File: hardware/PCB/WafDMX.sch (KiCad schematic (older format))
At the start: 16 parts

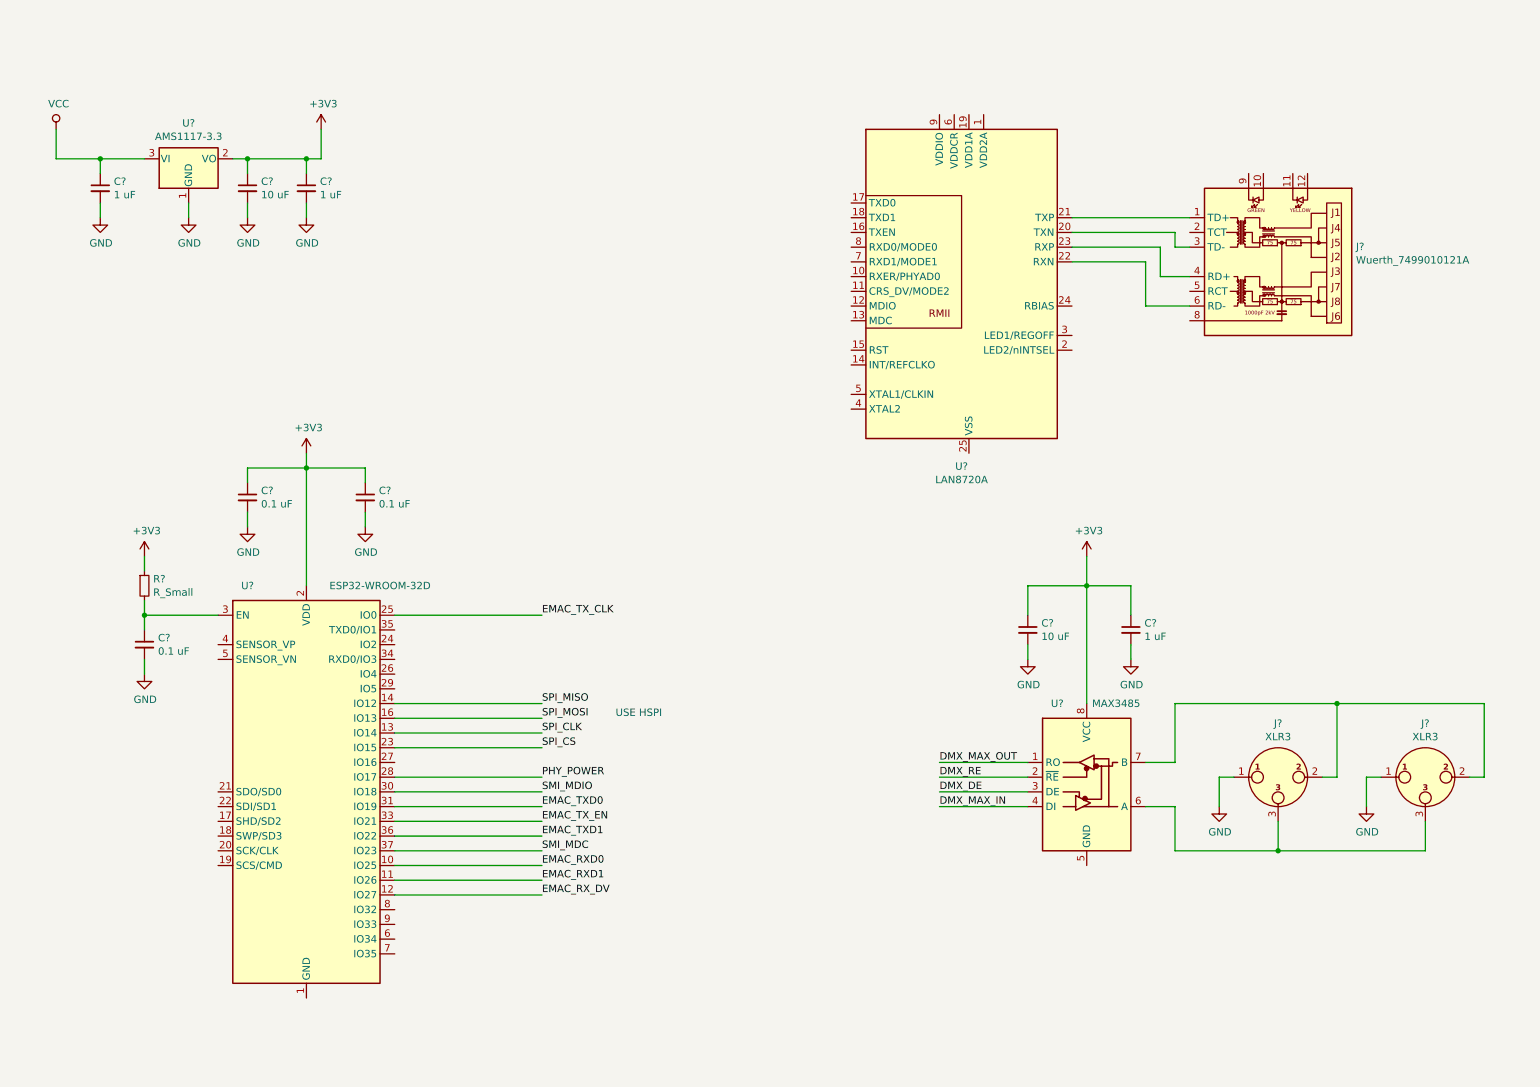
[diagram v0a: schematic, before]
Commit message: Add LAN8720A and trace
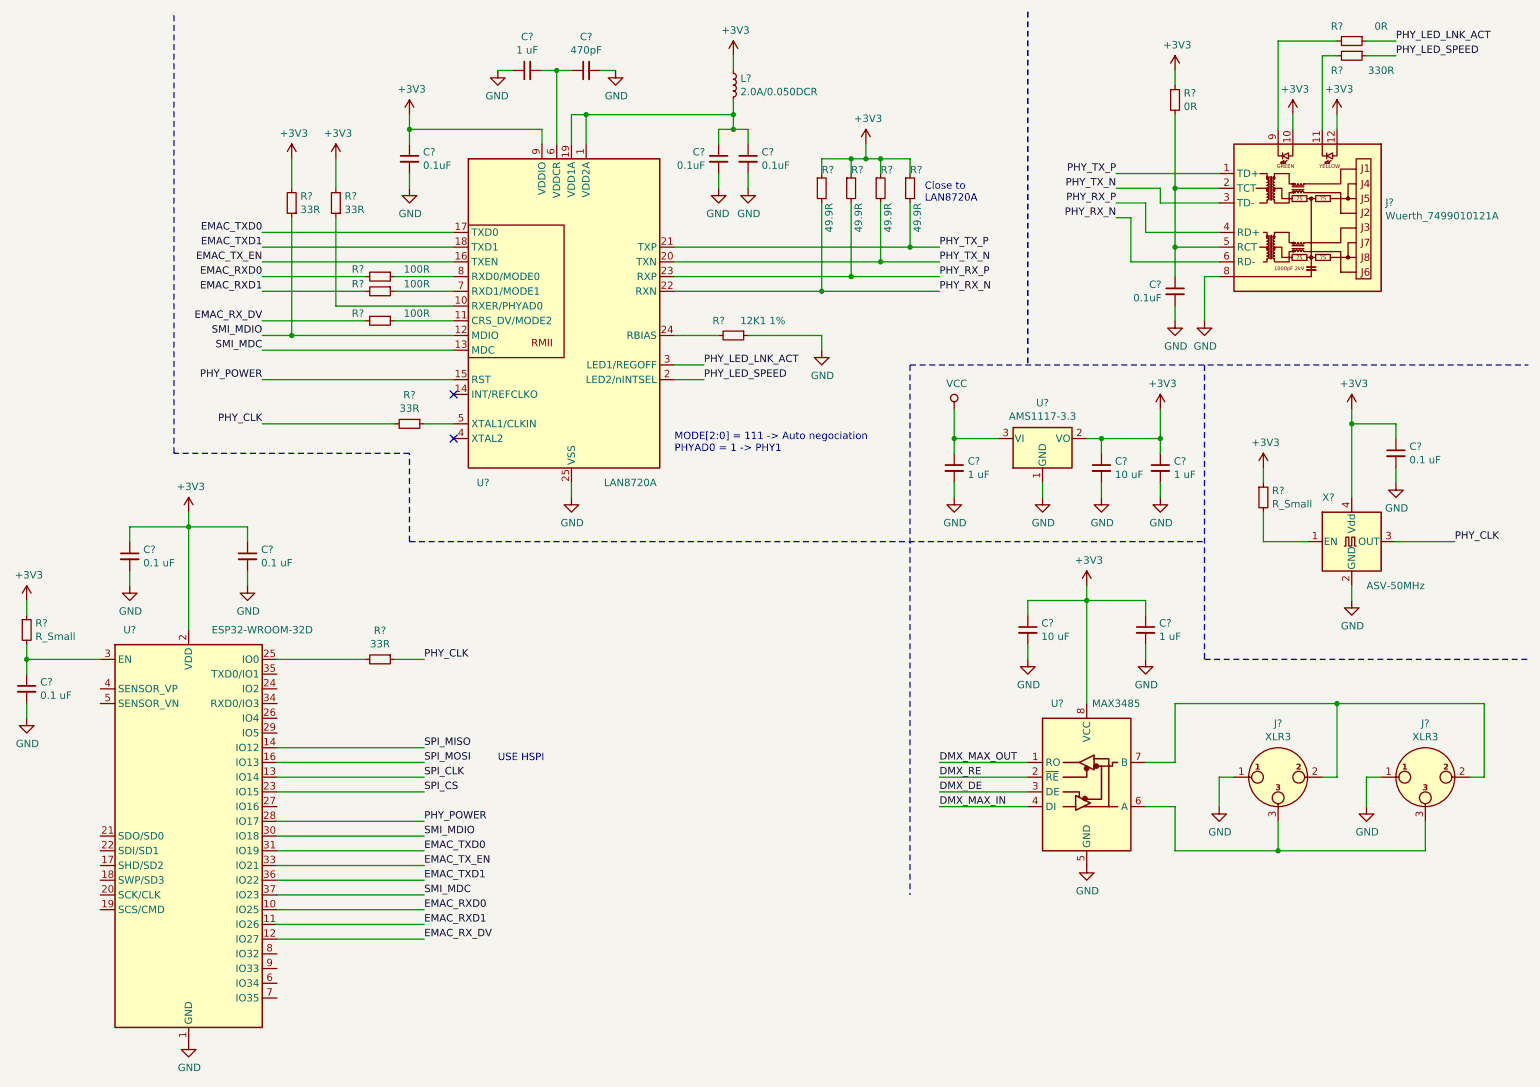
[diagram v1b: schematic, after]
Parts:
- added C? (x4): 0.1uF, symbol Device:C_Small
- added C?: 0.1 uF, symbol Device:C_Small
- added C?: 470pF, symbol Device:C_Small
- added C?: 1 uF, symbol Device:C_Small
- added L?: 2.0A/0.050DCR, symbol Device:L_Small
- added R? (x2): 0R, symbol Device:R_Small
- added R?: 330R, symbol Device:R_Small
- added R?: 12K1 1%, symbol Device:R_Small
- added R?: R_Small, symbol Device:R_Small
- added R? (x4): 33R, symbol Device:R_Small
- added R? (x4): 49.9R, symbol Device:R_Small
- added R? (x3): 100R, symbol Device:R_Small
- added X?: ASV-50MHz, Oscillator:Oscillator_SMD_Abracon_ASE-4Pin_3.2x2.5mm_HandSoldering, symbol Oscillator:ASV-xxxMHz
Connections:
- net +3V3: now also J?.10, J?.12, U?.9 (VDDIO), C?.1, C?.1, L?.1, R?.1, R?.1, R?.1, R?.1, R?.1, R?.1, R?.2, R?.2, X?.4 (Vdd)
- net EMAC_RXD0: now also R?.2
- net EMAC_RXD1: now also R?.2
- net EMAC_RX_DV: now also R?.2
- net EMAC_TXD0: now also U?.17 (TXD0)
- net EMAC_TXD1: now also U?.18 (TXD1)
- net EMAC_TX_EN: now also U?.16 (TXEN)
- net GND: now also J?.8, U?.1 (GND), U?.15 (GND), U?.25 (VSS), U?.38 (GND), U?.5 (GND), C?.1, C?.2, C?.2, C?.2, C?.2, C?.2, C?.2, R?.1, X?.2 (GND)
- net PHY_POWER: now also U?.15 (RST)
- net SMI_MDC: now also U?.13 (MDC)
- net SMI_MDIO: now also U?.12 (MDIO), R?.1
- net at U?.1 (VDD2A): now also U?.19 (VDD1A), C?.1, C?.1, L?.2
- net at U?.10 (RXER/PHYAD0): now also R?.1
- net at U?.11 (CRS_DV/MODE2): now also R?.1
- net PHY_LED_SPEED: now reaches U?.2 (LED2/nINTSEL)
- net PHY_LED_SPEED: now also R?.1
- net PHY_TX_N: now reaches J?.3 (TD-), U?.20 (TXN)
- net PHY_TX_N: now also R?.2
- net PHY_TX_P: now reaches J?.1 (TD+), U?.21 (TXP)
- net PHY_TX_P: now also R?.2
- net PHY_RX_N: now reaches J?.6 (RD-), U?.22 (RXN)
- net PHY_RX_N: now also R?.2
- net PHY_RX_P: now reaches J?.4 (RD+), U?.23 (RXP)
- net PHY_RX_P: now also R?.2
- net at U?.24 (RBIAS): now also R?.2
- net PHY_LED_LNK_ACT: now reaches U?.3 (LED1/REGOFF)
- net PHY_LED_LNK_ACT: now also R?.1
- net at U?.5 (XTAL1/CLKIN): now also R?.1
- net at U?.6 (VDDCR): now also C?.1, C?.2
- net at U?.7 (RXD1/MODE1): now also R?.1
- net at U?.8 (RXD0/MODE0): now also R?.1
- net at J?.11: now also R?.2
- net at J?.2 (TCT): now also J?.5 (RCT), C?.1, R?.2
- net at J?.9: now also R?.2
- net EMAC_TX_CLK: no longer names the net of U?.25 (IO0)
- net EMAC_TX_CLK: now also R?.2
- new net: R?.2, X?.1 (EN)
- new net PHY_CLK: R?.1, R?.2, X?.3 (OUT)
- no-connect marks 0 -> 2
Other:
- note added: "Close to\nLAN8720A"
- note added: "MODE[2:0] = 111 -> Auto negociation\nPHYAD0 = 1 -> PHY1\n"
- moved on the sheet: C?, J?, R?, U?

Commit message: Use A3 paper size, add CH340C
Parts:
- removed R? (x4): 49.9R, symbol Device:R_Small
- removed R? (x3): 100R, symbol Device:R_Small
- added C?: 0.01 uF, symbol Device:C_Small
- added C?: 0.1 uF, symbol Device:C_Small
- added C?: 22 uF, symbol Device:C_Small
- added J?: USB_B_Micro, Connector_USB:USB_Micro-B_Molex-105017-0001, symbol Connector:USB_B_Micro
- added J?: Screw_Terminal_01x02, TerminalBlock_Phoenix:TerminalBlock_Phoenix_MKDS-1,5-2_1x02_P5.00mm_Horizontal, symbol Connector:Screw_Terminal_01x02
- added Q? (x2): MMDT2222A, Package_TO_SOT_SMD:SOT-363_SC-70-6, symbol Transistor_BJT:MMDT2222A
- added R? (x2): 10K, symbol Device:R_Small
- added TP? (x13): TestPoint, TestPoint:TestPoint_Pad_1.0x1.0mm, symbol Connector:TestPoint
- added U?: CH340C, Package_SO:SOP-16_4.4x10.4mm_P1.27mm, symbol WafDMX:CH340C
- C?: value 10 uF -> 0.1 uF
- J?: footprint Connector_RJ:RJ45_Wuerth_7499151120_Horizontal -> Connector_RJ:RJ45_Wuerth_7499010121A_Horizontal
- R?: value R_Small -> 10K
- X?: footprint Oscillator:Oscillator_SMD_Abracon_ASE-4Pin_3.2x2.5mm_HandSoldering -> Oscillator:Oscillator_SMD_Abracon_ASV-4Pin_7.0x5.1mm
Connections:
- net +3V3: now also C?.1, C?.1, U?.16 (VCC); no longer R?.1
- net EMAC_RXD0: now also U?.8 (RXD0/MODE0)
- net EMAC_RXD1: now also U?.7 (RXD1/MODE1)
- net EMAC_RX_DV: now also U?.11 (CRS_DV/MODE2)
- net GND: now also R?.2, C?.2, C?.2, C?.2, J?.2 (Pin_2), J?.5 (GND), J?.6 (Shield), U?.1 (GND)
- net VCC: now also J?.1 (Pin_1)
- net at U?.17 (SHD/SD2): now also TP?.1
- net at U?.18 (SWP/SD3): now also TP?.1
- net at U?.19 (SCS/CMD): now also TP?.1
- net at U?.20 (SCK/CLK): now also TP?.1
- net at U?.21 (SDO/SD0): now also TP?.1
- net at U?.22 (SDI/SD1): now also TP?.1
- net at U?.24 (IO2): now also TP?.1
- net IO0: now reaches R?.2, U?.25 (IO0)
- net IO0: now also Q?.6 (C1)
- net at U?.26 (IO4): now also TP?.1
- net PHY_CLK_EN: now reaches U?.27 (IO16)
- net PHY_CLK_EN: now also R?.1, X?.1 (EN)
- net at U?.29 (IO5): now also TP?.1
- net EN: now reaches C?.1, R?.2, U?.3 (EN)
- net EN: now also Q?.4 (E2)
- net ESP32_RX: now reaches U?.34 (RXD0/IO3)
- net ESP32_RX: now also U?.2 (TXD)
- net ESP32_TX: now reaches U?.35 (TXD0/IO1)
- net ESP32_TX: now also U?.3 (RXD)
- net at U?.6 (IO34): now also TP?.1
- net at U?.7 (IO35): now also TP?.1
- net at U?.8 (IO32): now also TP?.1
- net at U?.9 (IO33): now also TP?.1
- new net: C?.1, U?.4 (V3)
- new net: Q?.2 (B1), R?.1
- new net: Q?.5 (B2), R?.1
- new net DTR: Q?.1 (E1), R?.2, U?.13 (DTR)
- new net RTS: Q?.3 (C2), R?.2, U?.14 (RTS)
- new net USB_DN: J?.2 (D-), U?.5 (UD_N)
- new net USB_DP: J?.3 (D+), U?.6 (UD_P)
- no-connect marks 2 -> 11
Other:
- note added: "All resistors MUST be close to LAN8720A"
- note removed: "Close to\nLAN8720A"
- moved on the sheet: C?, J?, L?, R?, U?, X?

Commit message: Place components
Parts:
- removed TP? (x4): TestPoint, TestPoint:TestPoint_Pad_1.0x1.0mm, symbol Connector:TestPoint
- added J4: Conn_01x04_Female, Connector_PinHeader_2.54mm:PinHeader_1x04_P2.54mm_Vertical, symbol Connector:Conn_01x04_Female
- added JP1: SolderJumper_2_Open, Jumper:SolderJumper-2_P1.3mm_Open_Pad1.0x1.5mm, symbol Jumper:SolderJumper_2_Open
- added P1, P2, P3, P4: POW_OUT, symbol WafDMX:POW_OUT
- added TP4, TP5: TestPoint, TestPoint:TestPoint_Pad_1.0x1.0mm, symbol Connector:TestPoint
- C1, C10, C11, C12, C14, C15, C16, C17, C18, C2, C6, C7, C9: renamed from C?; footprint (none) -> Capacitor_SMD:C_0603_1608Metric
- C13, C8: renamed from C?; footprint (none) -> Capacitor_SMD:C_1206_3216Metric
- C3, C4, C5: renamed from C?; value 0.1uF -> 0.1 uF; footprint (none) -> Capacitor_SMD:C_0603_1608Metric
- L1: renamed from L?; footprint (none) -> Inductor_SMD:L_0603_1608Metric
- R1, R10, R11, R12, R2, R3, R4, R5, R6, R7, R8: renamed from R?; footprint (none) -> Resistor_SMD:R_0603_1608Metric
- R9: renamed from R?; value R_Small -> 10K; footprint (none) -> Resistor_SMD:R_0603_1608Metric
- gave numbers to parts that had none: 21
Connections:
- net DMX_DE: now also U4.19 (SCS/CMD)
- net DMX_MAX_IN: now also U4.18 (SWP/SD3)
- net DMX_MAX_OUT: now also U4.17 (SHD/SD2)
- net DMX_RE: now also U4.20 (SCK/CLK)
- net GND: now also J2.1 (Pin_1), J4.4 (Pin_4); no longer J2.2 (Pin_2)
- net SPI_CLK: now also J4.2 (Pin_2)
- net SPI_MOSI: now also J4.3 (Pin_3)
- net VCC: now also J2.2 (Pin_2), JP1.1 (A), P1.~; no longer J2.1 (Pin_1)
- net at C4.1, C5.1, L1.2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: now also P4.~
- net at C1.2, C2.1, U2.6 (VDDCR): now also P2.~
- net at C11.1, U3.4 (V3): now also P3.~
- net SPI_CS: no longer names the net of U4.23 (IO15)
- net SPI_CS: now also TP5.1
- net SPI_MISO: no longer names the net of U4.14 (IO12)
- net SPI_MISO: now also TP4.1
- new net: J4.1 (Pin_1), JP1.2 (B)
- no-connect marks 11 -> 13
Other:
- moved on the sheet: J2

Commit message: Change Testpoints to TH, start placing
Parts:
- TP1, TP10, TP11, TP2, TP3, TP4, TP5, TP6, TP7, TP8, TP9: footprint TestPoint:TestPoint_Pad_1.0x1.0mm -> TestPoint:TestPoint_THTPad_1.0x1.0mm_Drill0.5mm
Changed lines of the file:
@@
 F 0 "TP1" V 4500 7300 50  0000 L CNN
 F 1 "TestPoint" V 4500 7575 50  0000 L CNN
-F 2 "TestPoint:TestPoint_Pad_1.0x1.0mm" H 4700 7100 50  0001 C CNN
+F 2 "TestPoint:TestPoint_THTPad_1.0x1.0mm_Drill0.5mm" H 4700 7100 50  0001 C CNN
 F 3 "~" H 4700 7100 50  0001 C CNN
 	1    4500 7100
@@
 F 0 "TP2" V 4500 7500 50  0000 L CNN
 F 1 "TestPoint" V 4500 7775 50  0000 L CNN
-F 2 "TestPoint:TestPoint_Pad_1.0x1.0mm" H 4700 7300 50  0001 C CNN
+F 2 "TestPoint:TestPoint_THTPad_1.0x1.0mm_Drill0.5mm" H 4700 7300 50  0001 C CNN
 F 3 "~" H 4700 7300 50  0001 C CNN
 	1    4500 7300
@@
 F 0 "TP3" V 4500 7600 50  0000 L CNN
 F 1 "TestPoint" V 4500 7875 50  0000 L CNN
-F 2 "TestPoint:TestPoint_Pad_1.0x1.0mm" H 4700 7400 50  0001 C CNN
+F 2 "TestPoint:TestPoint_THTPad_1.0x1.0mm_Drill0.5mm" H 4700 7400 50  0001 C CNN
 F 3 "~" H 4700 7400 50  0001 C CNN
 	1    4500 7400
@@
 F 0 "TP8" V 4500 9100 50  0000 L CNN
 F 1 "TestPoint" V 4500 9375 50  0000 L CNN
-F 2 "TestPoint:TestPoint_Pad_1.0x1.0mm" H 4700 8900 50  0001 C CNN
+F 2 "TestPoint:TestPoint_THTPad_1.0x1.0mm_Drill0.5mm" H 4700 8900 50  0001 C CNN
 F 3 "~" H 4700 8900 50  0001 C CNN
 	1    4500 8900
@@
 F 0 "TP9" V 4500 9200 50  0000 L CNN
 F 1 "TestPoint" V 4500 9475 50  0000 L CNN
-F 2 "TestPoint:TestPoint_Pad_1.0x1.0mm" H 4700 9000 50  0001 C CNN
+F 2 "TestPoint:TestPoint_THTPad_1.0x1.0mm_Drill0.5mm" H 4700 9000 50  0001 C CNN
 F 3 "~" H 4700 9000 50  0001 C CNN
 	1    4500 9000
@@
 F 0 "TP10" V 4500 9300 50  0000 L CNN
 F 1 "TestPoint" V 4500 9575 50  0000 L CNN
-F 2 "TestPoint:TestPoint_Pad_1.0x1.0mm" H 4700 9100 50  0001 C CNN
+F 2 "TestPoint:TestPoint_THTPad_1.0x1.0mm_Drill0.5mm" H 4700 9100 50  0001 C CNN
 F 3 "~" H 4700 9100 50  0001 C CNN
 	1    4500 9100
@@
 F 0 "TP11" V 4500 9400 50  0000 L CNN
 F 1 "TestPoint" V 4500 9675 50  0000 L CNN
-F 2 "TestPoint:TestPoint_Pad_1.0x1.0mm" H 4700 9200 50  0001 C CNN
+F 2 "TestPoint:TestPoint_THTPad_1.0x1.0mm_Drill0.5mm" H 4700 9200 50  0001 C CNN
 F 3 "~" H 4700 9200 50  0001 C CNN
 	1    4500 9200
@@
 F 0 "TP6" V 1600 8300 50  0000 L CNN
 F 1 "TestPoint" V 1600 8575 50  0000 L CNN
-F 2 "TestPoint:TestPoint_Pad_1.0x1.0mm" H 1800 8100 50  0001 C CNN
+F 2 "TestPoint:TestPoint_THTPad_1.0x1.0mm_Drill0.5mm" H 1800 8100 50  0001 C CNN
 F 3 "~" H 1800 8100 50  0001 C CNN
 	1    1600 8100
@@
 F 0 "TP7" V 1600 8400 50  0000 L CNN
 F 1 "TestPoint" V 1600 8675 50  0000 L CNN
-F 2 "TestPoint:TestPoint_Pad_1.0x1.0mm" H 1800 8200 50  0001 C CNN
+F 2 "TestPoint:TestPoint_THTPad_1.0x1.0mm_Drill0.5mm" H 1800 8200 50  0001 C CNN
 F 3 "~" H 1800 8200 50  0001 C CNN
 	1    1600 8200
@@
 F 0 "TP4" V 4500 7700 50  0000 L CNN
 F 1 "TestPoint" V 4500 7975 50  0000 L CNN
-F 2 "TestPoint:TestPoint_Pad_1.0x1.0mm" H 4700 7500 50  0001 C CNN
+F 2 "TestPoint:TestPoint_THTPad_1.0x1.0mm_Drill0.5mm" H 4700 7500 50  0001 C CNN
 F 3 "~" H 4700 7500 50  0001 C CNN
 	1    4500 7500
@@
 F 0 "TP5" V 4500 8000 50  0000 L CNN
 F 1 "TestPoint" V 4500 8275 50  0000 L CNN
-F 2 "TestPoint:TestPoint_Pad_1.0x1.0mm" H 4700 7800 50  0001 C CNN
+F 2 "TestPoint:TestPoint_THTPad_1.0x1.0mm_Drill0.5mm" H 4700 7800 50  0001 C CNN
 F 3 "~" H 4700 7800 50  0001 C CNN
 	1    4500 7800

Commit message: Add routing
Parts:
- C1, C10, C11, C12, C13, C14, C15, C16, C17, C18, C2, C3, C4, C5, C6, C7, C8, C9: symbol Device:C_Small -> WafDMX-rescue:C_Small-Device
- J1: symbol Connector:Wuerth_7499010121A -> WafDMX-rescue:Wuerth_7499010121A-Connector
- J2: footprint TerminalBlock_Phoenix:TerminalBlock_Phoenix_MKDS-1,5-2_1x02_P5.00mm_Horizontal -> WafDMX:TerminalBlock_WAGO_2604-1102_2x05_P5.00mm_30Degree; symbol Connector:Screw_Terminal_01x02 -> WafDMX-rescue:Screw_Terminal_01x02-Connector
- J3: symbol Connector:USB_B_Micro -> WafDMX-rescue:USB_B_Micro-Connector
- J4: symbol Connector:Conn_01x04_Female -> WafDMX-rescue:Conn_01x04_Female-Connector
- J5: footprint (none) -> WafDMX:XLR_Neutrik_NC3FAAH_Horizontal; symbol Connector:XLR3 -> WafDMX-rescue:XLR3-Connector
- J6: footprint (none) -> WafDMX:XLR_Neutrik_NC3MAAH_Horizontal; symbol Connector:XLR3 -> WafDMX-rescue:XLR3-Connector
- JP1: symbol Jumper:SolderJumper_2_Open -> WafDMX-rescue:SolderJumper_2_Open-Jumper
- L1: symbol Device:L_Small -> WafDMX-rescue:L_Small-Device
- Q1: symbol Transistor_BJT:MMDT2222A -> WafDMX-rescue:MMDT2222A-Transistor_BJT
- R1, R10, R11, R12, R2, R5, R6, R7, R8, R9: symbol Device:R_Small -> WafDMX-rescue:R_Small-Device
- R3, R4: value 33R -> 10K; symbol Device:R_Small -> WafDMX-rescue:R_Small-Device
- TP1, TP10, TP11, TP2, TP3, TP4, TP5, TP6, TP7, TP8, TP9: symbol Connector:TestPoint -> WafDMX-rescue:TestPoint-Connector
- U1: symbol Regulator_Linear:AMS1117-3.3 -> WafDMX-rescue:AMS1117-3.3-Regulator_Linear
- U2: symbol Interface_Ethernet:LAN8720A -> WafDMX-rescue:LAN8720A-Interface_Ethernet
- U4: symbol RF_Module:ESP32-WROOM-32D -> WafDMX-rescue:ESP32-WROOM-32D-RF_Module
- U5: symbol Interface_UART:MAX3485 -> WafDMX-rescue:MAX3485-Interface_UART
- X1: symbol Oscillator:ASV-xxxMHz -> WafDMX-rescue:ASV-xxxMHz-Oscillator

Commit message: Add 3V3-5V level shifter
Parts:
- removed TP6: TestPoint, TestPoint:TestPoint_THTPad_1.0x1.0mm_Drill0.5mm, symbol WafDMX-rescue:TestPoint-Connector
- added C19, C20: 0.1 uF, Capacitor_SMD:C_0603_1608Metric, symbol WafDMX-rescue:C_Small-Device-WafDMX-rescue
- added R13: R_Small, Resistor_SMD:R_0603_1608Metric, symbol Device:R_Small
- added U6: TXB0102DCU, Package_SO:VSSOP-8_2.4x2.1mm_P0.5mm, symbol Logic_LevelTranslator:TXB0102DCU
- C1, C10, C11, C12, C13, C14, C15, C16, C17, C18, C2, C3, C4, C5, C6, C7, C8, C9: symbol WafDMX-rescue:C_Small-Device -> WafDMX-rescue:C_Small-Device-WafDMX-rescue
- J1: symbol WafDMX-rescue:Wuerth_7499010121A-Connector -> WafDMX-rescue:Wuerth_7499010121A-Connector-WafDMX-rescue
- J2: symbol WafDMX-rescue:Screw_Terminal_01x02-Connector -> WafDMX-rescue:Screw_Terminal_01x02-Connector-WafDMX-rescue
- J3: symbol WafDMX-rescue:USB_B_Micro-Connector -> WafDMX-rescue:USB_B_Micro-Connector-WafDMX-rescue
- J4: symbol WafDMX-rescue:Conn_01x04_Female-Connector -> WafDMX-rescue:Conn_01x04_Female-Connector-WafDMX-rescue
- J5, J6: symbol WafDMX-rescue:XLR3-Connector -> WafDMX-rescue:XLR3-Connector-WafDMX-rescue
- JP1: symbol WafDMX-rescue:SolderJumper_2_Open-Jumper -> WafDMX-rescue:SolderJumper_2_Open-Jumper-WafDMX-rescue
- L1: symbol WafDMX-rescue:L_Small-Device -> WafDMX-rescue:L_Small-Device-WafDMX-rescue
- Q1: symbol WafDMX-rescue:MMDT2222A-Transistor_BJT -> WafDMX-rescue:MMDT2222A-Transistor_BJT-WafDMX-rescue
- R1, R10, R11, R12, R2, R3, R4, R5, R6, R7, R8, R9: symbol WafDMX-rescue:R_Small-Device -> WafDMX-rescue:R_Small-Device-WafDMX-rescue
- TP1, TP10, TP11, TP2, TP3, TP4, TP5, TP7, TP8, TP9: symbol WafDMX-rescue:TestPoint-Connector -> WafDMX-rescue:TestPoint-Connector-WafDMX-rescue
- U1: symbol WafDMX-rescue:AMS1117-3.3-Regulator_Linear -> WafDMX-rescue:AMS1117-3.3-Regulator_Linear-WafDMX-rescue
- U2: symbol WafDMX-rescue:LAN8720A-Interface_Ethernet -> WafDMX-rescue:LAN8720A-Interface_Ethernet-WafDMX-rescue
- U4: symbol WafDMX-rescue:ESP32-WROOM-32D-RF_Module -> WafDMX-rescue:ESP32-WROOM-32D-RF_Module-WafDMX-rescue
- U5: symbol WafDMX-rescue:MAX3485-Interface_UART -> WafDMX-rescue:MAX3485-Interface_UART-WafDMX-rescue
- X1: symbol WafDMX-rescue:ASV-xxxMHz-Oscillator -> WafDMX-rescue:ASV-xxxMHz-Oscillator-WafDMX-rescue
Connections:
- net +3V3: now also C19.1, U6.3 (VCCA)
- net GND: now also C19.2, C20.2, R13.2, U6.2 (GND)
- net SPI_CLK: now also U6.4 (A2); no longer J4.2 (Pin_2)
- net SPI_MOSI: now also U6.5 (A1); no longer J4.3 (Pin_3)
- net VCC: now also C20.1, U6.7 (VCCB)
- net SPI_OE: now reaches U4.21 (SDO/SD0)
- net SPI_OE: now also R13.1, U6.6 (OE)
- new net 5V_SPI_CLK: J4.2 (Pin_2), U6.1 (B2)
- new net 5V_SPI_MOSI: J4.3 (Pin_3), U6.8 (B1)

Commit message: Add farnell references
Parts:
- C1, C18, C7, C9: Part Number (none) -> 2470425
- C10, C12, C14, C15, C16, C17, C19, C20, C3, C4, C5, C6: Part Number (none) -> 2688469
- C11: Part Number (none) -> 2470432
- C13: Part Number (none) -> 1735533
- C2: Part Number (none) -> 8819904
- C8: Part Number (none) -> 2672214RL
- J1: Part Number (none) -> 1636379
- J2: Part Number (none) -> 2821984
- J3: Part Number (none) -> 2293836
- J4, JP1, L1, P1, P2, P3, P4, TP1, TP10, TP11, TP2, TP3, TP4, TP5, TP7, TP8, TP9, U1, U3, U4: Part Number (none) -> -
- J5: Part Number (none) -> 724518
- J6: Part Number (none) -> 724543
- Q1: Part Number (none) -> 2317636
- R1, R5: Part Number (none) -> 1469739
- R10, R8: Part Number (none) -> 9238301
- R11, R12, R13, R3, R4, R6, R9: Part Number (none) -> 2303192
- R2: Part Number (none) -> 1469803
- R7: Part Number (none) -> 2447244
- U2: Part Number (none) -> 2292578
- U5: Part Number (none) -> 2512100
- U6: Part Number (none) -> 2295723
- X1: Part Number (none) -> 1611840
